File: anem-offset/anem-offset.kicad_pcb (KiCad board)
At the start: 2 copper layers, 82.5 x 69.8 mm, 34 parts, among them IC1 LM336, Q1 TIP120, U1 LM324, U2 LM358

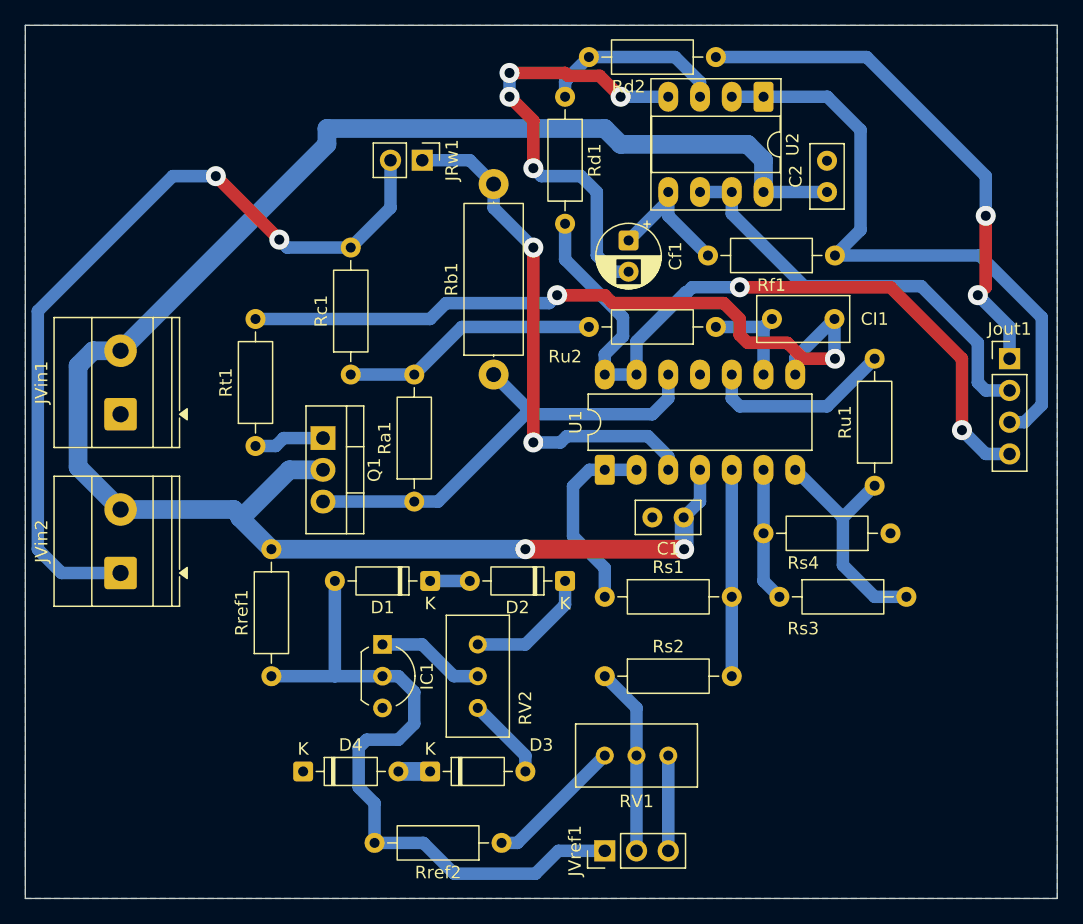
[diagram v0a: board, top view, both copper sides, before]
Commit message: Pequenas correções e melhorias
 * Furos de montagem
 * Valores 'mais corretos' dos componentes.
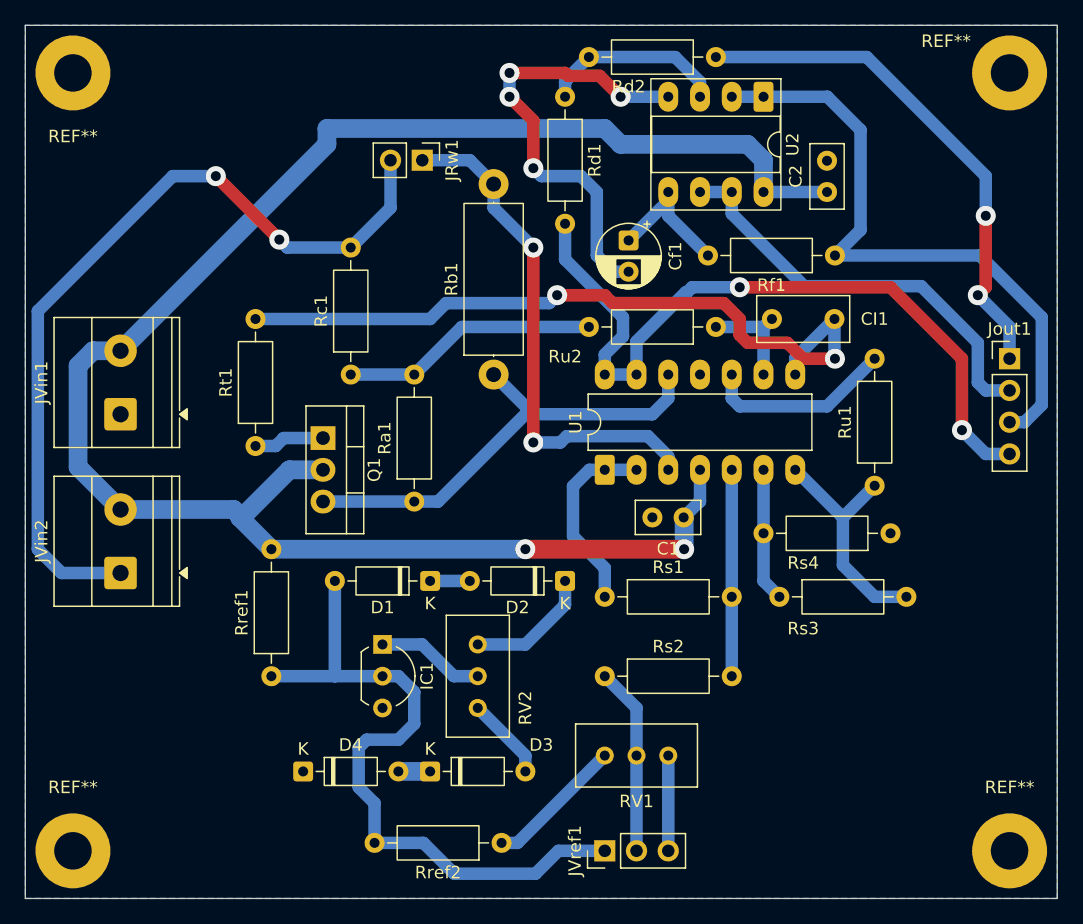
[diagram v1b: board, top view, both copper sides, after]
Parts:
- added REF**: MountingHole_3mm_Pad, MountingHole:MountingHole_3mm_Pad, F.Cu at (22.9, 29.2)
- added REF**: MountingHole_3mm_Pad, MountingHole:MountingHole_3mm_Pad, F.Cu at (97.8, 29.2)
- added REF**: MountingHole_3mm_Pad, MountingHole:MountingHole_3mm_Pad, F.Cu at (22.9, 91.4)
- added REF**: MountingHole_3mm_Pad, MountingHole:MountingHole_3mm_Pad, F.Cu at (97.8, 91.4)
- CI1: value C -> 1n
- RV2, Rd2, Rs1, Rs2: value 1k -> 10k
- Rd1: value 1k -> 20k
- Rf1: value 10k -> 15k
- Rref1: value 1.2k -> 3.9k
